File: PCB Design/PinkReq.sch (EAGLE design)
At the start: 7 parts

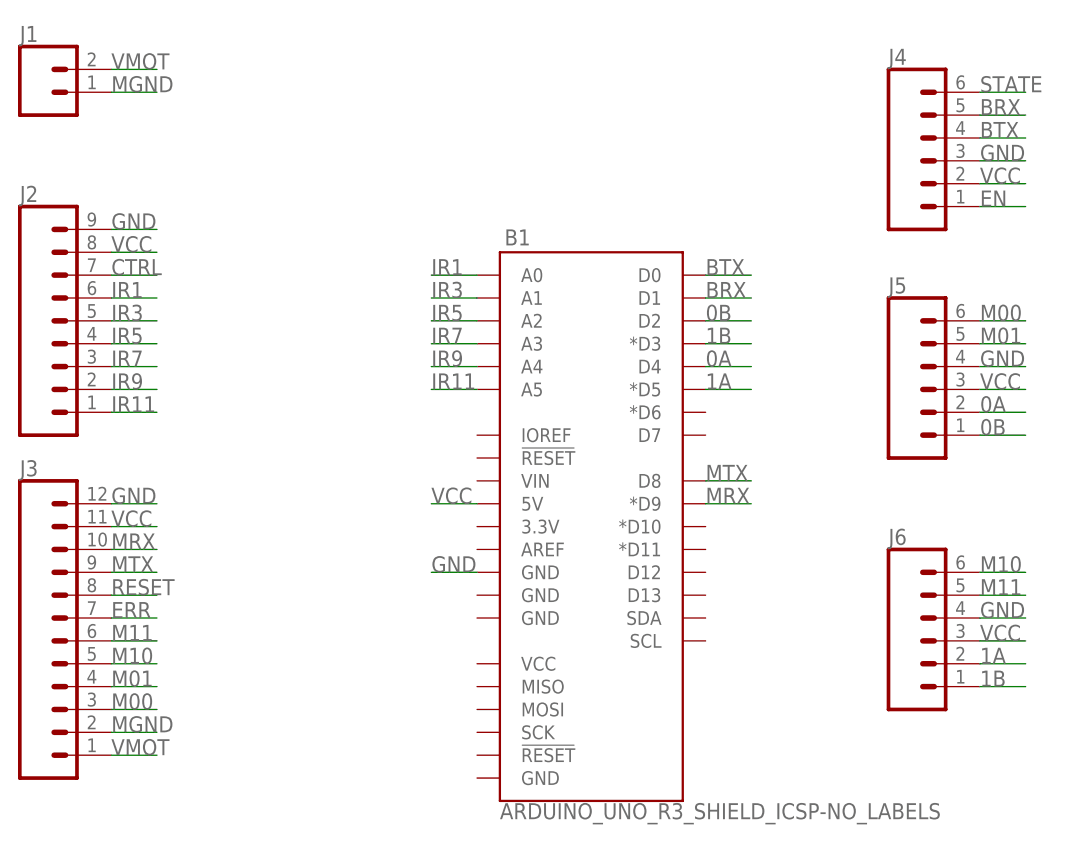
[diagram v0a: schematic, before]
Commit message: PCB updated with SR04
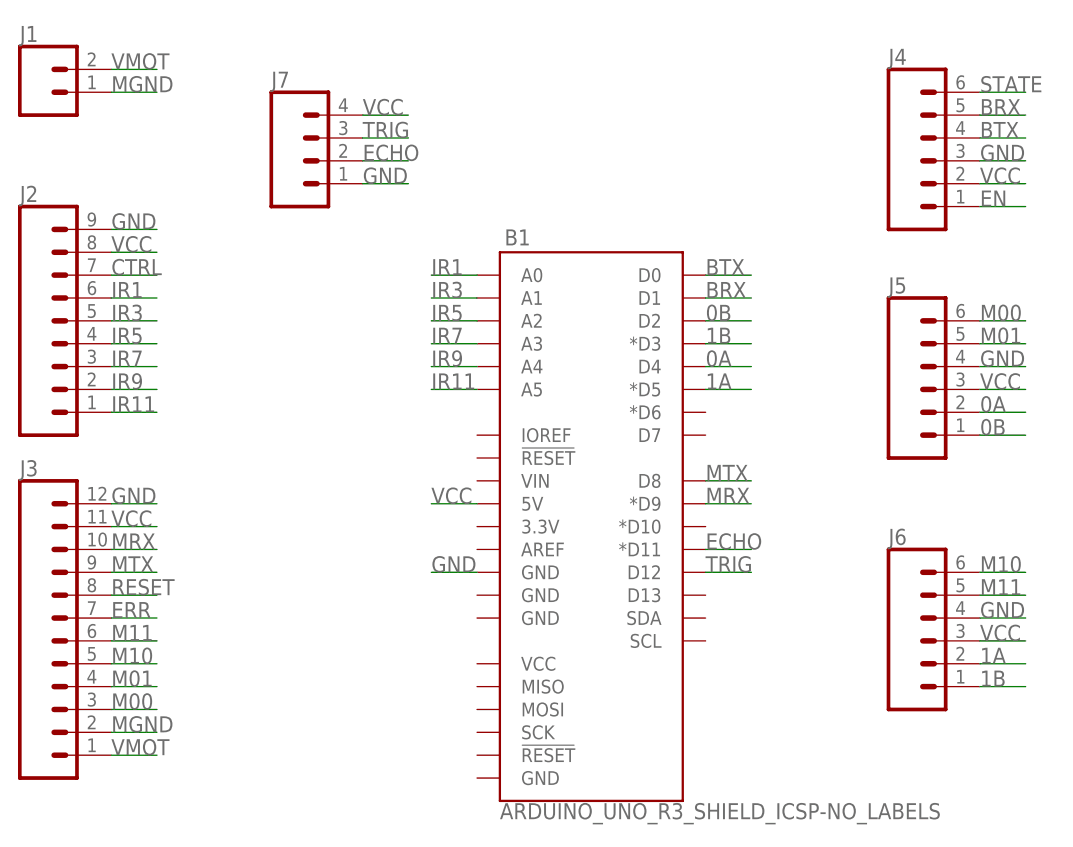
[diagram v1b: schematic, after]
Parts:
- added J7: (no value), SparkFun-Connectors:CONN_04LOCK
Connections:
- new net ECHO: B1.*D11, J7.2
- new net TRIG: B1.D12, J7.3
- net GND: now also J7.1
- net VCC: now also J7.4
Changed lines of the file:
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@@
 <part name="J6" library="SparkFun-Connectors" library_urn="urn:adsk.eagle:library:513" deviceset="CONN_06" device="FEMALE_LOCK" package3d_urn="urn:adsk.eagle:package:38124/1"/>
 <part name="J1" library="SparkFun-Connectors" library_urn="urn:adsk.eagle:library:513" deviceset="CONN_02" device="5MM" package3d_urn="urn:adsk.eagle:package:38044/1"/>
+<part name="J7" library="SparkFun-Connectors" library_urn="urn:adsk.eagle:library:513" deviceset="CONN_04" device="LOCK" package3d_urn="urn:adsk.eagle:package:38089/1"/>
 </parts>
 <sheets>
@@
 <attribute name="NAME" x="10.16" y="94.488" size="1.778" layer="95" font="vector"/>
 </instance>
+<instance part="J7" gate="G$1" x="43.18" y="81.28" smashed="yes">
+<attribute name="VALUE" x="38.1" y="73.914" size="1.778" layer="96" font="vector"/>
+<attribute name="NAME" x="38.1" y="89.408" size="1.778" layer="95" font="vector"/>
+</instance>
 </instances>
 <busses>
@@
 <label x="116.84" y="30.48" size="1.778" layer="95"/>
 </segment>
+<segment>
+<pinref part="J7" gate="G$1" pin="1"/>
+<wire x1="48.26" y1="78.74" x2="53.34" y2="78.74" width="0.1524" layer="91"/>
+<label x="48.26" y="78.74" size="1.778" layer="95"/>
+</segment>
 </net>
 <net name="VCC" class="0">
@@
 <label x="116.84" y="27.94" size="1.778" layer="95"/>
 </segment>
+<segment>
+<pinref part="J7" gate="G$1" pin="4"/>
+<wire x1="48.26" y1="86.36" x2="53.34" y2="86.36" width="0.1524" layer="91"/>
+<label x="48.26" y="86.36" size="1.778" layer="95"/>
+</segment>
 </net>
 <net name="CTRL" class="0">
@@
 </segment>
 </net>
+<net name="TRIG" class="0">
+<segment>
+<pinref part="J7" gate="G$1" pin="3"/>
+<wire x1="48.26" y1="83.82" x2="53.34" y2="83.82" width="0.1524" layer="91"/>
+<label x="48.26" y="83.82" size="1.778" layer="95"/>
+</segment>
+<segment>
+<pinref part="B1" gate="G$1" pin="D12"/>
+<wire x1="86.36" y1="35.56" x2="91.44" y2="35.56" width="0.1524" layer="91"/>
+<label x="86.36" y="35.56" size="1.778" layer="95"/>
+</segment>
+</net>
+<net name="ECHO" class="0">
+<segment>
+<pinref part="J7" gate="G$1" pin="2"/>
+<wire x1="48.26" y1="81.28" x2="53.34" y2="81.28" width="0.1524" layer="91"/>
+<label x="48.26" y="81.28" size="1.778" layer="95"/>
+</segment>
+<segment>
+<pinref part="B1" gate="G$1" pin="*D11"/>
+<wire x1="86.36" y1="38.1" x2="91.44" y2="38.1" width="0.1524" layer="91"/>
+<label x="86.36" y="38.1" size="1.778" layer="95"/>
+</segment>
+</net>

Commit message: PCB and Qik w/ BT added
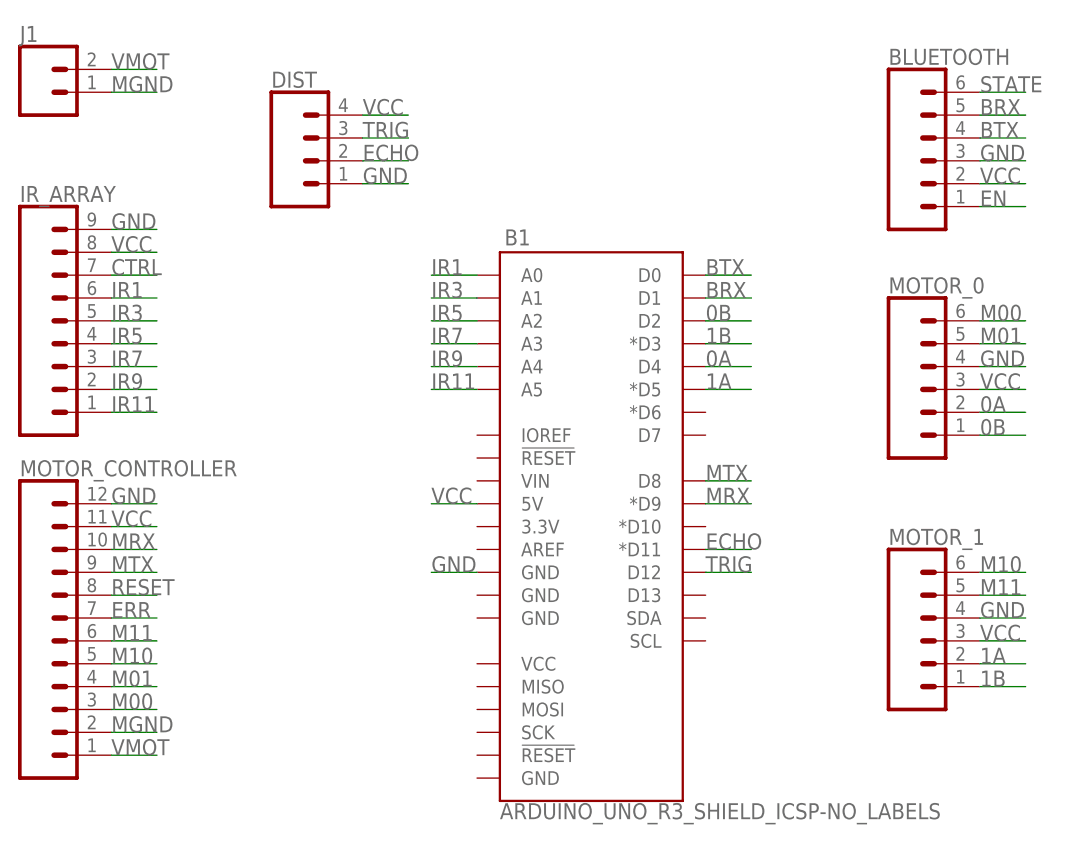
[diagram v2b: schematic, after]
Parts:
- renumbered J2 to IR_ARRAY, J3 to MOTOR_CONTROLLER, J4 to BLUETOOTH, J5 to MOTOR_0, J6 to MOTOR_1, J7 to DIST
